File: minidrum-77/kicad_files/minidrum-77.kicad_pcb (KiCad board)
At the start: 2 copper layers, 50 x 101.6 mm, 47 parts, among them J1 TRIG_IN, J2 AUDIO_OUT, J3 EXT_COIL, SW1 LPF/HPF_IN, SW2 RS/C, SW3 C6_SEL, SW4 COIL_1, SW5 COIL_2, SW6 C11_SEL, SW7 C8_SEL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

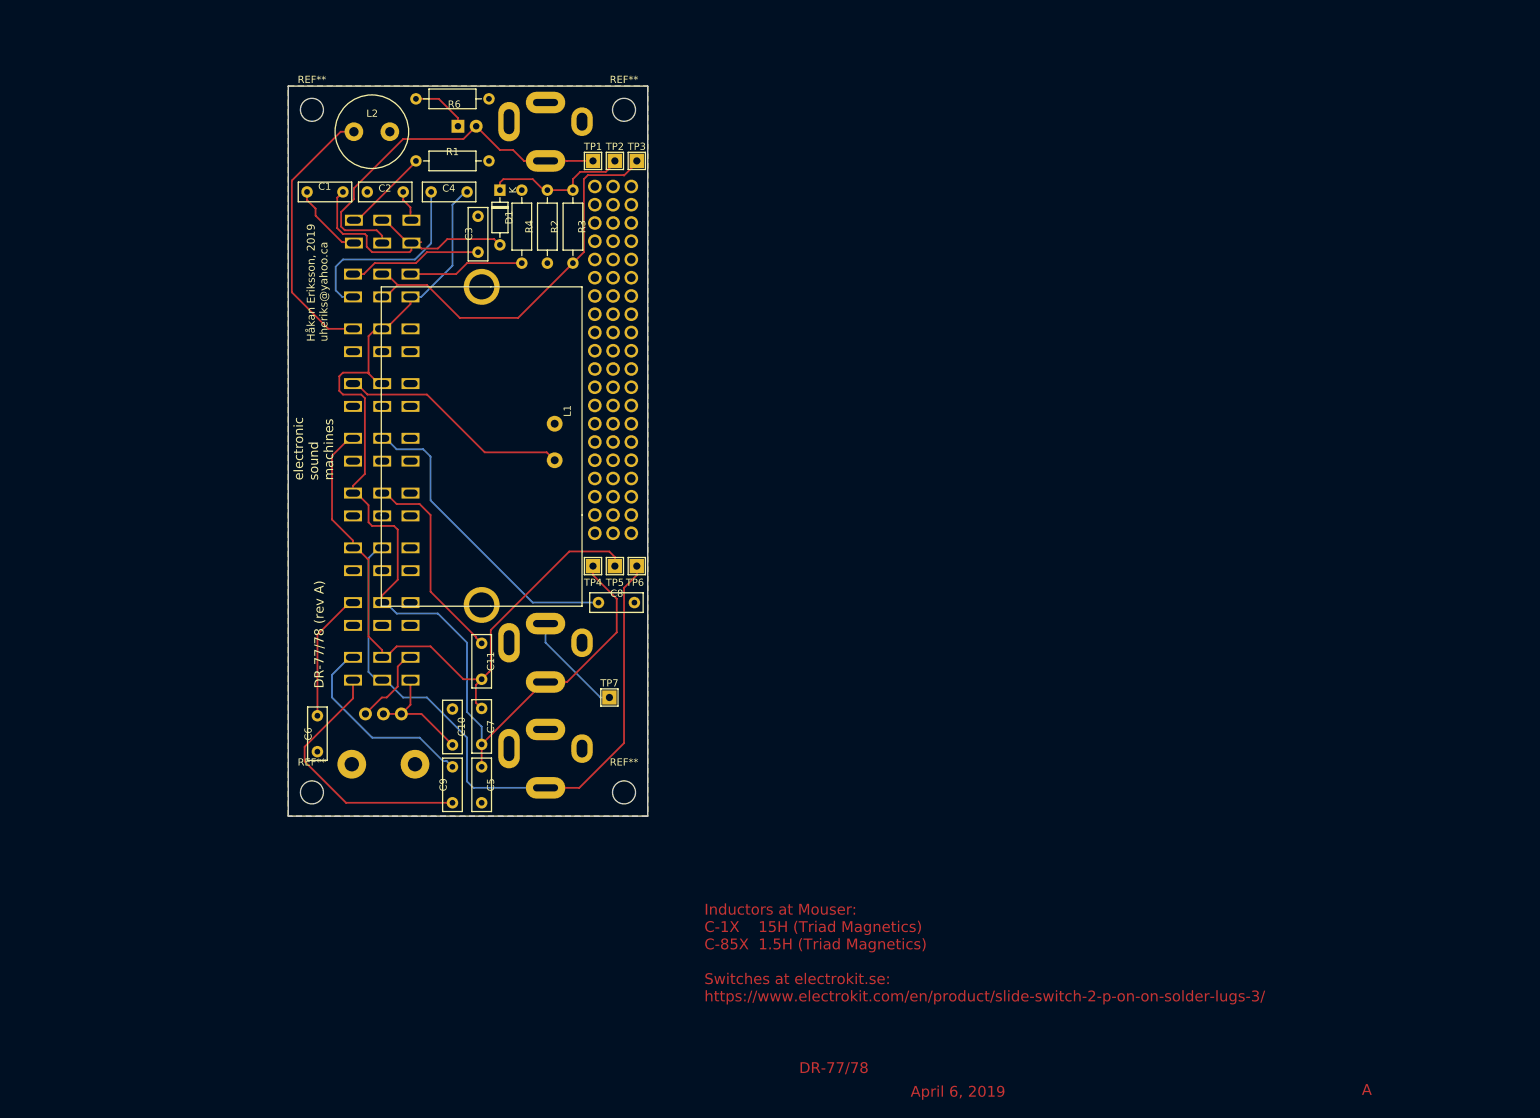
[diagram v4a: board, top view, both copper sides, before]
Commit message: minidrum: Move switches apart a bit
Experiments with PCB layout on paper indicated that the
space between switches was too tight. Maybe still, but better.

Also cleaning up other PCBs a bit.
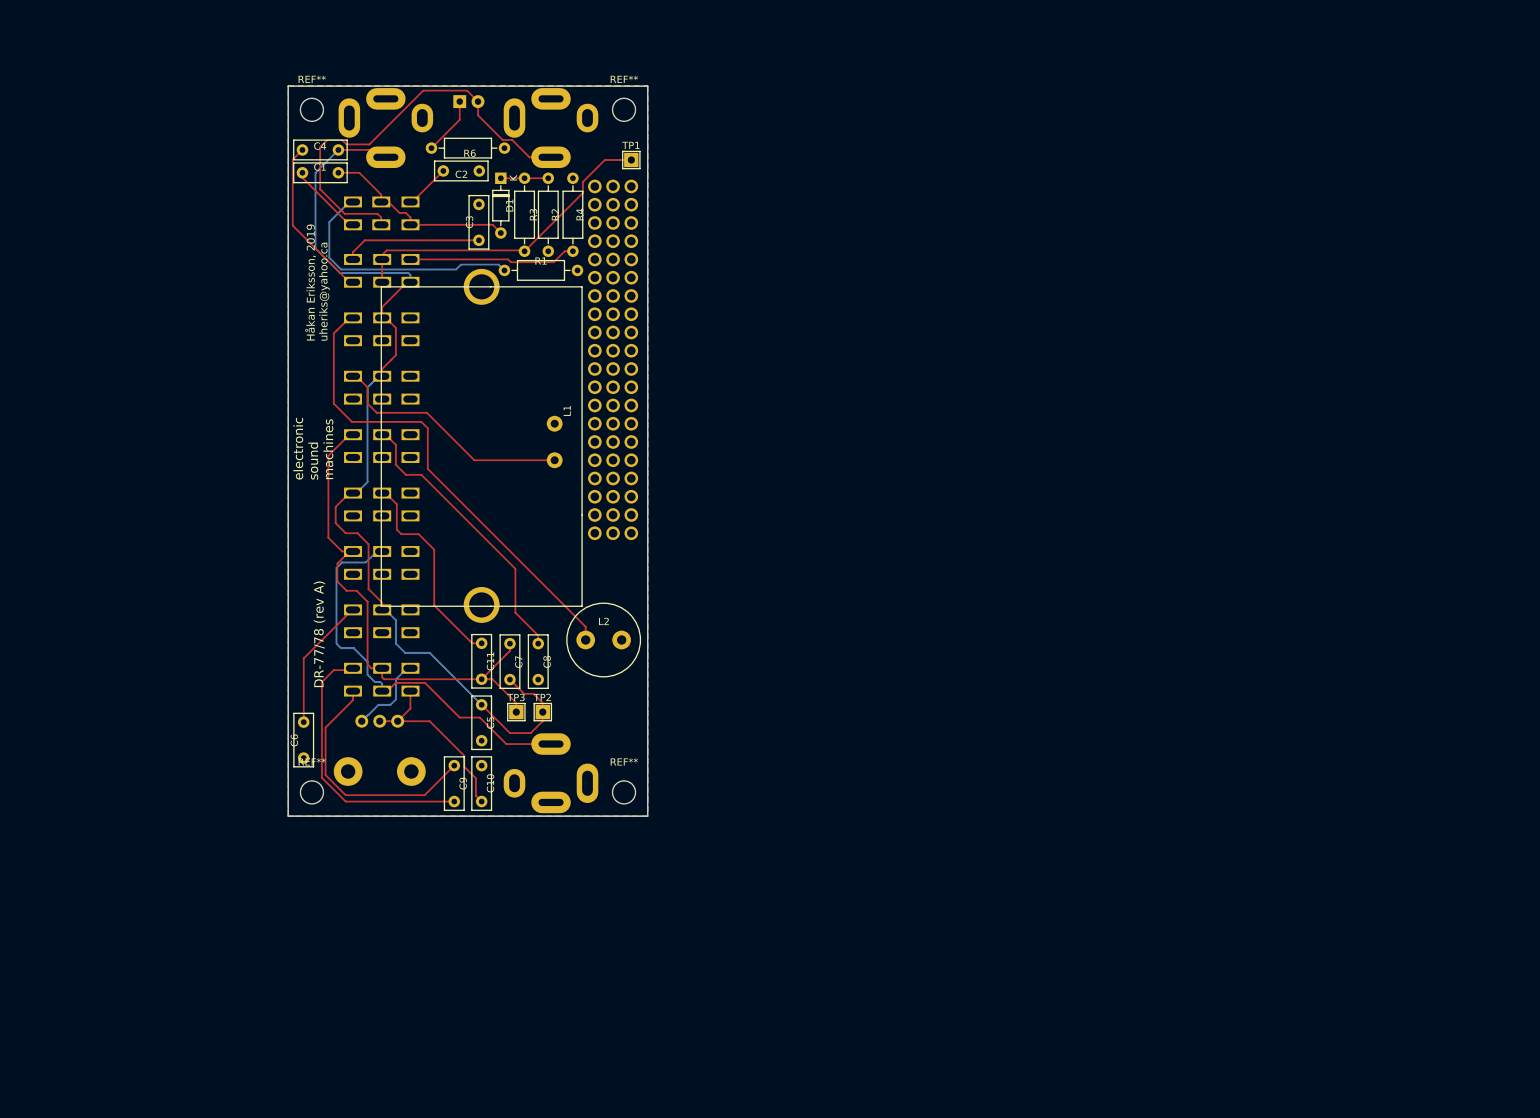
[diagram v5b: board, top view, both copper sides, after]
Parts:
- removed TP4, TP5, TP6: , TestPoint:TestPoint_THTPad_2.0x2.0mm_Drill1.0mm
- removed TP7: DEFAULT_EXT_COIL, TestPoint:TestPoint_THTPad_2.0x2.0mm_Drill1.0mm
- moved TP3 78.5 mm to (153.7, 140.2)
- moved L2 77.7 mm to (163.3, 130.2)
- moved TP2 77.4 mm to (157.4, 140.2)
- moved J3 76.3 mm to (130.4, 64.6)
- moved R1 19.6 mm to (152.0, 78.7)
- moved C4 18.8 mm to (128.9, 62.0)
- moved J2 14.4 mm to (163.6, 143.0), turned to 180 degrees
- moved C8 10.1 mm to (156.7, 130.7), turned to 270 degrees
- moved C7 9.84 mm to (152.8, 130.7)
- moved C10 8.86 mm to (148.8, 152.7)
- moved C5 8.64 mm to (148.8, 139.2)
- moved R4 7.30 mm to (161.5, 76.1)
- moved R6 7.19 mm to (141.9, 61.7)
- moved R3 6.93 mm to (154.8, 76.1)
- moved C2 6.31 mm to (143.5, 64.9), turned to 0 degrees
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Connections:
- TP1 pad 1: Net-(D2-Pad2) -> Net-(R3-Pad1)
- TP2 pad 1: Net-(D1-Pad1) -> Net-(C4-Pad1)
- TP3 pad 1: Net-(R3-Pad1) -> Net-(C11-Pad1)
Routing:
- net Net-(J2-Pad3): track 92.1 -> 56.2 mm
- net Net-(L2-Pad1): track 37.6 -> 66.4 mm
- net Net-(R1-Pad1): track 12.1 -> 35.1 mm
- net Net-(C11-Pad1): track 87.1 -> 71.0 mm
- net Net-(J3-Pad2): track 14.7 -> 0.00 mm
- net Net-(D1-Pad1): track 20.6 -> 6.60 mm
- net Net-(C4-Pad1): track 148.4 -> 134.9 mm
- net Net-(C1-Pad1): track 39.5 -> 27.3 mm
- net Net-(R3-Pad1): track 56.0 -> 44.9 mm
- net Net-(C9-Pad1): track 27.8 -> 38.1 mm
- net Net-(C10-Pad1): track 16.6 -> 25.8 mm
- net Net-(R4-Pad1): track 16.1 -> 23.4 mm
- net Net-(C4-Pad2): track 28.1 -> 22.7 mm
- net Net-(D2-Pad2): track 53.2 -> 57.9 mm
- net Net-(C8-Pad1): track 43.1 -> 39.6 mm
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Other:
- board text added: "Inductors at Mouser: C-1X 15H (Triad Magnetics) C-85X 1.5H (Triad Magnetics) Switches at electrokit.se: https://www.electrokit.com/en/product/slide-switch-2-p-on-on-solder-lugs-3/ Jacks and pots at Thonk: Jacks, PJ301BM: https://www.thonk.co.uk/shop/3-5mm-jacks/ Pots: https://www.thonk.co.uk/shop/alpha-9mm-pots/"
- board text added: "The kind of drum sound sounds used in Roland CR-78 and TR-77 (and others), for e.g. BD, RS, Claves, etc. – read the service manuals! Adapted to Eurorack by Håkan Eriksson Revision A, prototype-ish."
- board text removed: "Inductors at Mouser: C-1X 15H (Triad Magnetics) C-85X 1.5H (Triad Magnetics) Switches at electrokit.se: https://www.electrokit.com/en/product/slide-switch-2-p-on-on-solder-lugs-3/"
